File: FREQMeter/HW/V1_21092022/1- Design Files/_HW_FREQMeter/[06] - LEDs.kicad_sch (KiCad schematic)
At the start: 40 parts

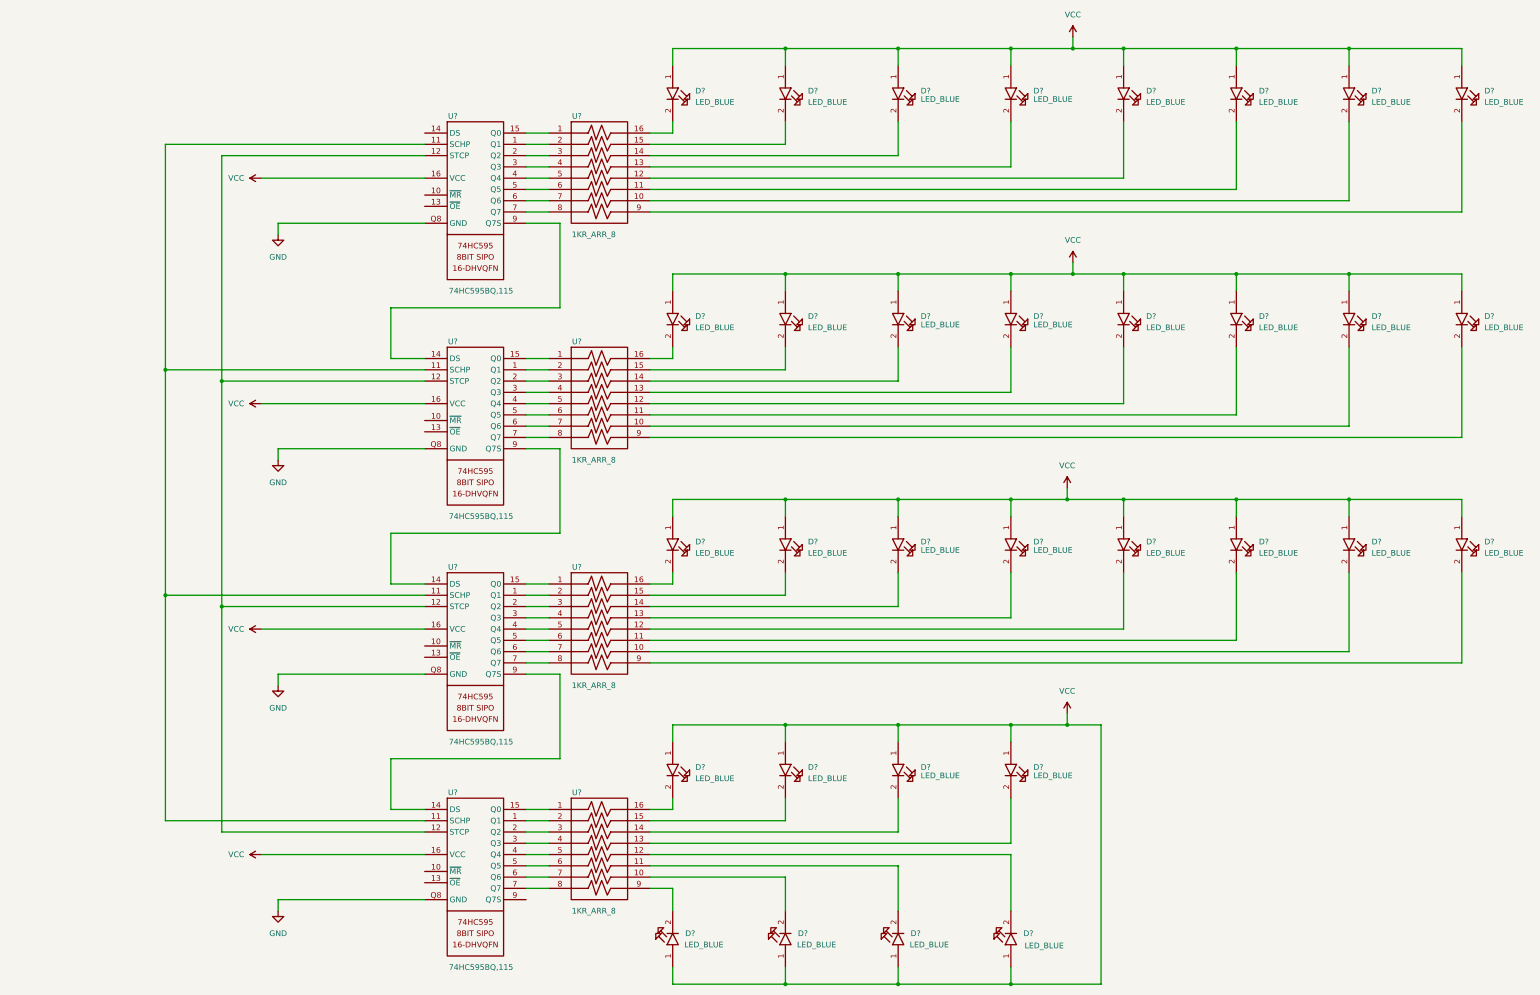
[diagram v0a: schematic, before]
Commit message: progress on Frequency meter hardware
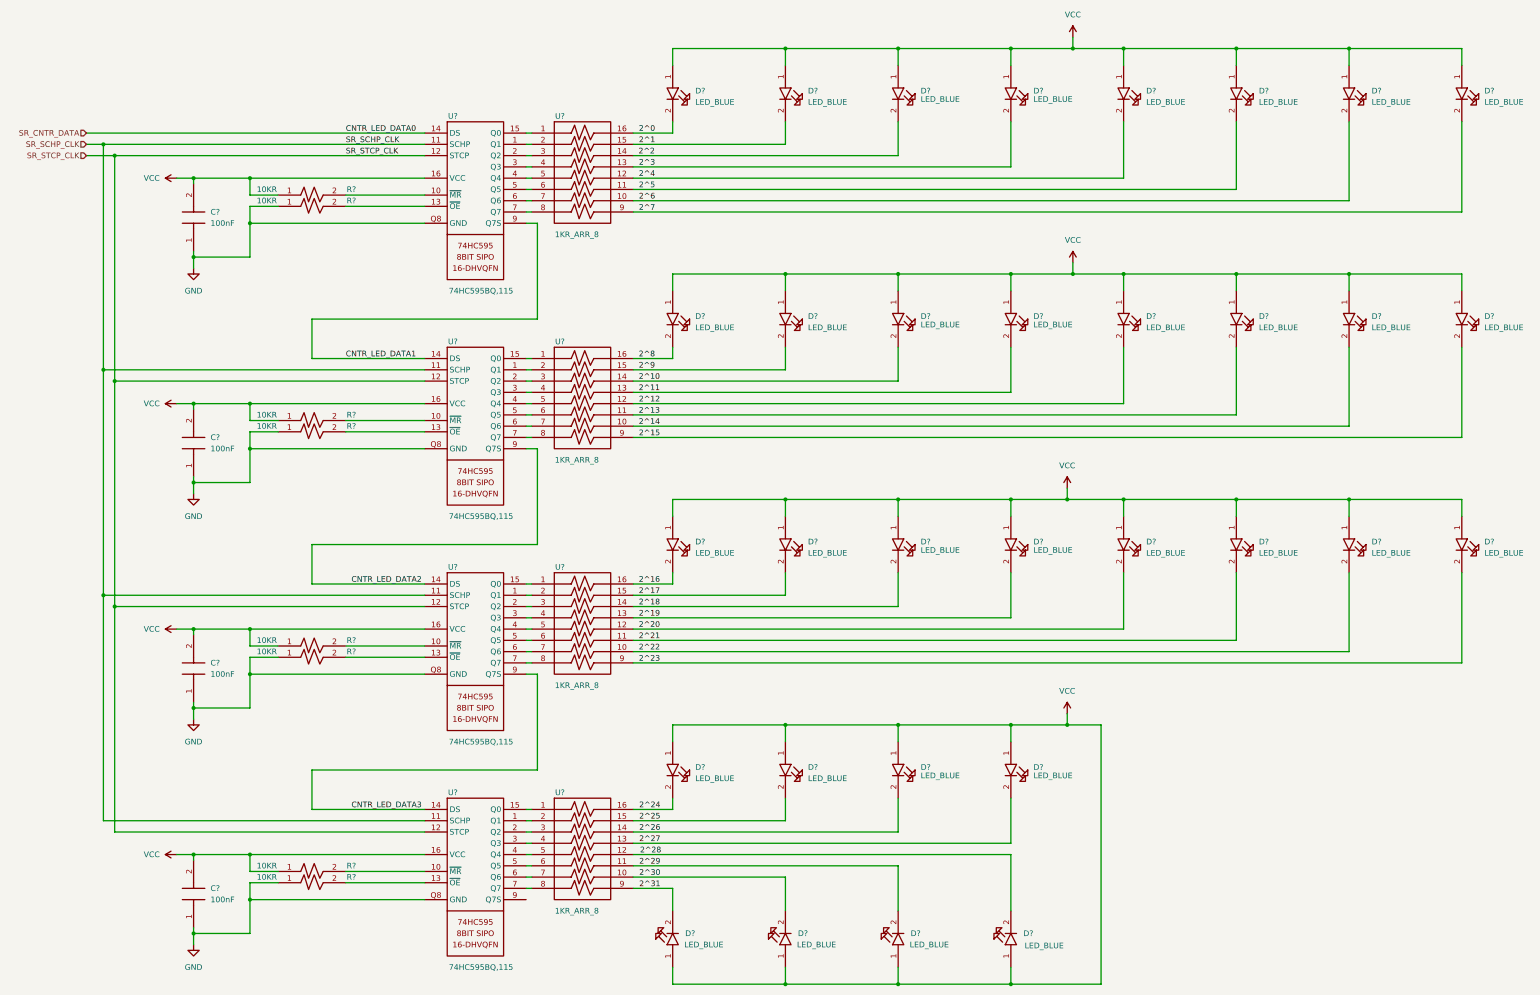
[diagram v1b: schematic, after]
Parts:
- added C? (x4): 100nF, symbol FREQMeter:100nF
- added R? (x8): 10KR, symbol FREQMeter:10KR
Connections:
- net GND: now also C?.1, C?.1, C?.1, C?.1, R?.1, R?.1, R?.1, R?.1
- net VCC: now also C?.2, C?.2, C?.2, C?.2, R?.1, R?.1, R?.1, R?.1
- net 2^8: now reaches D?.2, U?.16
- net at U?.10 (~{MR}): now also R?.2 (x4)
- net SR_SCHP_CLK: now reaches U?.11 (SCHP), U?.11 (SCHP), U?.11 (SCHP), U?.11 (SCHP)
- net SR_STCP_CLK: now reaches U?.12 (STCP), U?.12 (STCP), U?.12 (STCP), U?.12 (STCP)
- net at U?.13 (~{OE}): now also R?.2 (x4)
- net SR_CNTR_DATA: now reaches U?.14 (DS)
- net CNTR_LED_DATA1: now reaches U?.14 (DS), U?.9 (Q7S)
- net 2^9: now reaches D?.2, U?.15
- net 2^6: now reaches D?.2, U?.10
- net 2^19: now reaches D?.2, U?.13
- net 2^5: now reaches D?.2, U?.11
- net 2^27: now reaches D?.2, U?.13
- net 2^30: now reaches D?.2, U?.10
- net 2^28: now reaches D?.2, U?.12
- net 2^11: now reaches D?.2, U?.13
- net 2^12: now reaches D?.2, U?.12
- net 2^31: now reaches D?.2, U?.9
- net 2^4: now reaches D?.2, U?.12
- net 2^3: now reaches D?.2, U?.13
- net 2^2: now reaches D?.2, U?.14
- net 2^1: now reaches D?.2, U?.15
- net 2^0: now reaches D?.2, U?.16
- net 2^7: now reaches D?.2, U?.9
- net 2^16: now reaches D?.2, U?.16
- net 2^22: now reaches D?.2, U?.10
- net 2^18: now reaches D?.2, U?.14
- net 2^17: now reaches D?.2, U?.15
- net 2^14: now reaches D?.2, U?.10
- net 2^13: now reaches D?.2, U?.11
- net 2^10: now reaches D?.2, U?.14
- net 2^15: now reaches D?.2, U?.9
- net 2^29: now reaches D?.2, U?.11
- net 2^23: now reaches D?.2, U?.9
- net CNTR_LED_DATA3: now reaches U?.14 (DS), U?.9 (Q7S)
- net 2^21: now reaches D?.2, U?.11
- net 2^20: now reaches D?.2, U?.12
- net CNTR_LED_DATA2: now reaches U?.14 (DS), U?.9 (Q7S)
- net 2^26: now reaches D?.2, U?.14
- net 2^25: now reaches D?.2, U?.15
- net 2^24: now reaches D?.2, U?.16
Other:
- moved on the sheet: U?
